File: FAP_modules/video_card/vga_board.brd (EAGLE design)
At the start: 100 x 75 mm, 32 parts, among them IC1 IS61LV256, IC2 IS61LV256

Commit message: added interrupt chaining and WAIT
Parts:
- moved U$2 12.4 mm to (3.05, 59.4)
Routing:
- net VGA_VSYNC: track 72.4 -> 84.3 mm
- net N$2: track 14.3 -> 25.8 mm
- net VGA_HSYNC: track 76.4 -> 87.6 mm
- net N$4: track 12.0 -> 18.8 mm
- net N$6: track 16.2 -> 14.2 mm
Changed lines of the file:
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@@
 <circle x="21.59" y="68.58" radius="2.032" width="0" layer="41"/>
 <circle x="92.71" y="68.58" radius="2.032" width="0" layer="41"/>
-<circle x="8.128" y="34.5186" radius="2.794" width="0" layer="41"/>
-<circle x="8.128" y="59.5884" radius="3.048" width="0" layer="41"/>
-<text x="1.27" y="65.2018" size="1.6764" layer="25" distance="70">FAP80 VGA
+<circle x="8.0772" y="46.8884" radius="2.794" width="0" layer="41"/>
+<circle x="8.0772" y="71.882" radius="3.048" width="0" layer="41"/>
+<text x="1.3716" y="29.1592" size="1.6764" layer="25" distance="70">FAP80 VGA
 Video Card REV2
 dekuNukem 2016</text>
@@
 <attribute name="NAME" x="27.051" y="54.0639" size="0.8128" layer="25" rot="R180"/>
 </element>
-<element name="U$2" library="SparkFun-Connectors" package="DB15" value="DB15" x="3.048" y="47.0154" smashed="yes" rot="R90"/>
+<element name="U$2" library="SparkFun-Connectors" package="DB15" value="DB15" x="3.048" y="59.4106" smashed="yes" rot="R90"/>
 <element name="U$1" library="cpu_board" package="FAP_BUS_2X38" value="FAP_BUS_FAP_BUS" x="32.258" y="2.032" smashed="yes"/>
 <element name="IC1" library="61lv256" package="SOJ28/3_LONGPAD" value="IS61LV256" x="46.228" y="51.816" smashed="yes" rot="R270">
@@
 <wire x1="22.341" y1="38.2524" x2="21.441" y2="37.3524" width="0.3048" layer="1"/>
 <wire x1="21.441" y1="37.3524" x2="19.558" y2="37.3524" width="0.3048" layer="1"/>
-<wire x1="19.558" y1="37.3524" x2="17.791" y2="37.3524" width="0.3048" layer="1"/>
-<wire x1="10.67" y1="42.6954" x2="10.668" y2="42.6954" width="0.3048" layer="1"/>
-<wire x1="17.791" y1="37.3524" x2="12.448" y2="42.6954" width="0.3048" layer="1"/>
-<wire x1="12.448" y1="42.6954" x2="10.668" y2="42.6954" width="0.3048" layer="1"/>
+<wire x1="19.558" y1="37.3524" x2="17.41" y2="37.3524" width="0.3048" layer="1"/>
+<wire x1="17.41" y1="37.3524" x2="15.2908" y2="39.4716" width="0.3048" layer="1"/>
+<wire x1="15.2908" y1="39.4716" x2="15.2908" y2="50.4678" width="0.3048" layer="1"/>
+<wire x1="15.2908" y1="50.4678" x2="10.668" y2="55.0906" width="0.3048" layer="1"/>
 </signal>
 <signal name="GND">
@@
 <wire x1="22.341" y1="45.8724" x2="19.569" y2="45.8724" width="0.3048" layer="1"/>
 <wire x1="19.569" y1="45.8724" x2="19.558" y2="45.8614" width="0.3048" layer="1"/>
-<wire x1="19.558" y1="45.8614" x2="18.682" y2="44.9854" width="0.3048" layer="1"/>
-<wire x1="18.682" y1="44.9854" x2="10.668" y2="44.9854" width="0.3048" layer="1"/>
+<wire x1="19.569" y1="45.8724" x2="18.2118" y2="45.8724" width="0.3048" layer="1"/>
+<wire x1="18.2118" y1="45.8724" x2="16.8402" y2="47.244" width="0.3048" layer="1"/>
+<wire x1="16.8402" y1="47.244" x2="16.8402" y2="51.2084" width="0.3048" layer="1"/>
+<wire x1="16.8402" y1="51.2084" x2="10.668" y2="57.3806" width="0.3048" layer="1"/>
 </signal>
 <signal name="N$5">
@@
 <wire x1="22.341" y1="53.6194" x2="22.33" y2="53.6084" width="0.3048" layer="1"/>
 <wire x1="22.33" y1="53.6084" x2="19.558" y2="53.6084" width="0.3048" layer="1"/>
-<wire x1="19.558" y1="53.6084" x2="19.039" y2="53.6084" width="0.3048" layer="1"/>
-<wire x1="19.039" y1="53.6084" x2="17.018" y2="51.5874" width="0.3048" layer="1"/>
-<wire x1="17.018" y1="51.5874" x2="17.018" y2="48.4124" width="0.3048" layer="1"/>
-<wire x1="10.674" y1="47.2694" x2="10.668" y2="47.2754" width="0.3048" layer="1"/>
-<wire x1="17.018" y1="48.4124" x2="15.881" y2="47.2754" width="0.3048" layer="1"/>
-<wire x1="15.881" y1="47.2754" x2="10.668" y2="47.2754" width="0.3048" layer="1"/>
+<wire x1="19.558" y1="53.6084" x2="18.2736" y2="53.6084" width="0.3048" layer="1"/>
+<wire x1="18.2736" y1="53.6084" x2="12.192" y2="59.69" width="0.3048" layer="1"/>
+<wire x1="12.192" y1="59.69" x2="10.6874" y2="59.69" width="0.3048" layer="1"/>
+<wire x1="10.6874" y1="59.69" x2="10.668" y2="59.6706" width="0.3048" layer="1"/>
 </signal>
 <signal name="+3V3">
@@
 <contactref element="U$2" pad="14"/>
 <contactref element="U$3" pad="23"/>
-<wire x1="1.651" y1="47.6504" x2="3.556" y2="49.5554" width="0.3048" layer="16"/>
-<wire x1="3.556" y1="49.5554" x2="5.578" y2="49.5554" width="0.3048" layer="16"/>
-<wire x1="5.578" y1="49.5554" x2="5.588" y2="49.5654" width="0.3048" layer="16"/>
 <wire x1="46.99" y1="15.24" x2="46.99" y2="17.8308" width="0.3048" layer="16"/>
 <wire x1="46.99" y1="17.8308" x2="46.101" y2="18.7198" width="0.3048" layer="16"/>
 <wire x1="46.101" y1="18.7198" x2="11.1506" y2="18.7198" width="0.3048" layer="16"/>
 <wire x1="11.1506" y1="18.7198" x2="1.651" y2="28.2194" width="0.3048" layer="16"/>
-<wire x1="1.651" y1="28.2194" x2="1.651" y2="47.6504" width="0.3048" layer="16"/>
+<wire x1="1.651" y1="28.2194" x2="1.651" y2="58.0236" width="0.3048" layer="16"/>
+<wire x1="1.651" y1="58.0236" x2="5.588" y2="61.9606" width="0.3048" layer="16"/>
 </signal>
 <signal name="VGA_VSYNC">
 <contactref element="U$2" pad="13"/>
 <contactref element="U$3" pad="21"/>
-<wire x1="3.0226" y1="45.593" x2="4.699" y2="47.2694" width="0.3048" layer="16"/>
-<wire x1="4.699" y1="47.2694" x2="5.582" y2="47.2694" width="0.3048" layer="16"/>
-<wire x1="5.582" y1="47.2694" x2="5.588" y2="47.2754" width="0.3048" layer="16"/>
 <wire x1="49.53" y1="15.24" x2="49.53" y2="17.3736" width="0.3048" layer="16"/>
 <wire x1="49.53" y1="17.3736" x2="47.0662" y2="19.8374" width="0.3048" layer="16"/>
 <wire x1="47.0662" y1="19.8374" x2="13.6652" y2="19.8374" width="0.3048" layer="16"/>
 <wire x1="13.6652" y1="19.8374" x2="3.0226" y2="30.48" width="0.3048" layer="16"/>
-<wire x1="3.0226" y1="30.48" x2="3.0226" y2="45.593" width="0.3048" layer="16"/>
+<wire x1="3.0226" y1="30.48" x2="3.0226" y2="57.1052" width="0.3048" layer="16"/>
+<wire x1="3.0226" y1="57.1052" x2="5.588" y2="59.6706" width="0.3048" layer="16"/>
 </signal>
 <signal name="+V">

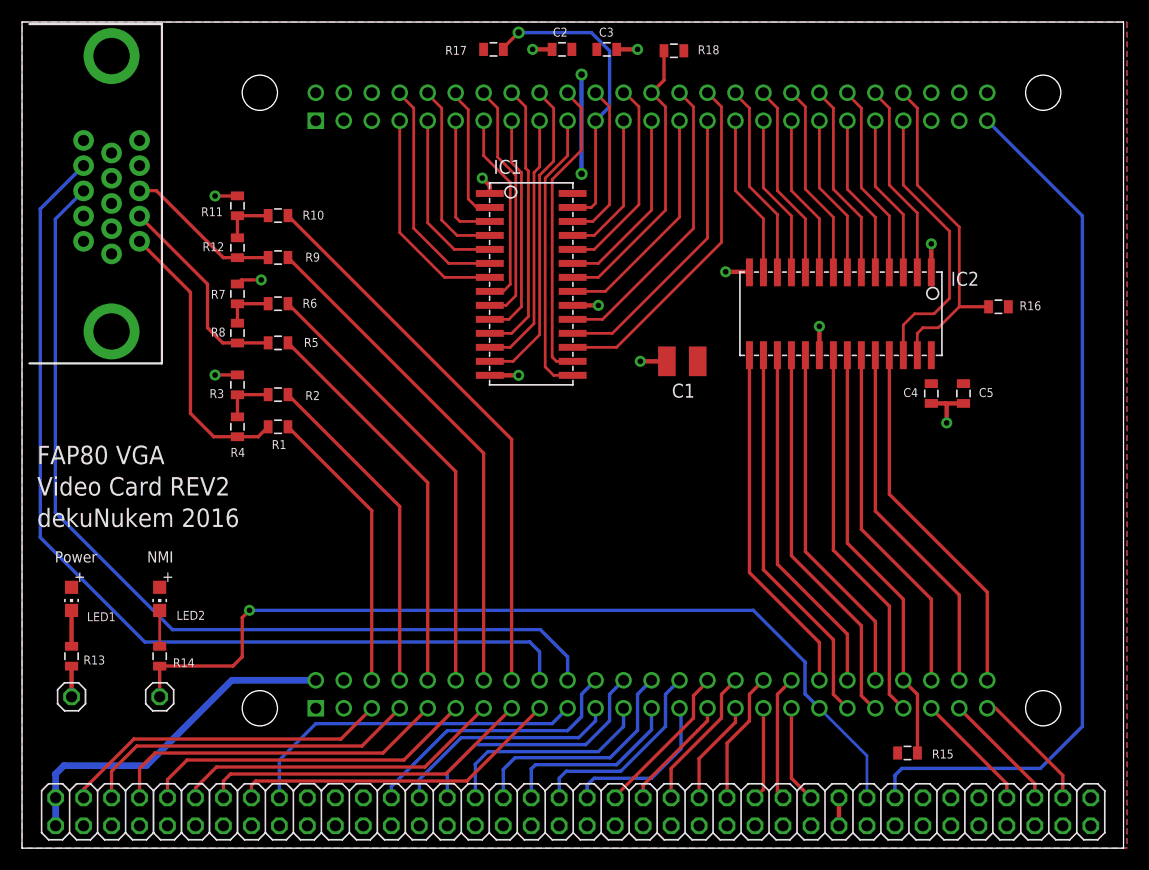
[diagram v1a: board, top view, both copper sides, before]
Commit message: moved VGA sockect
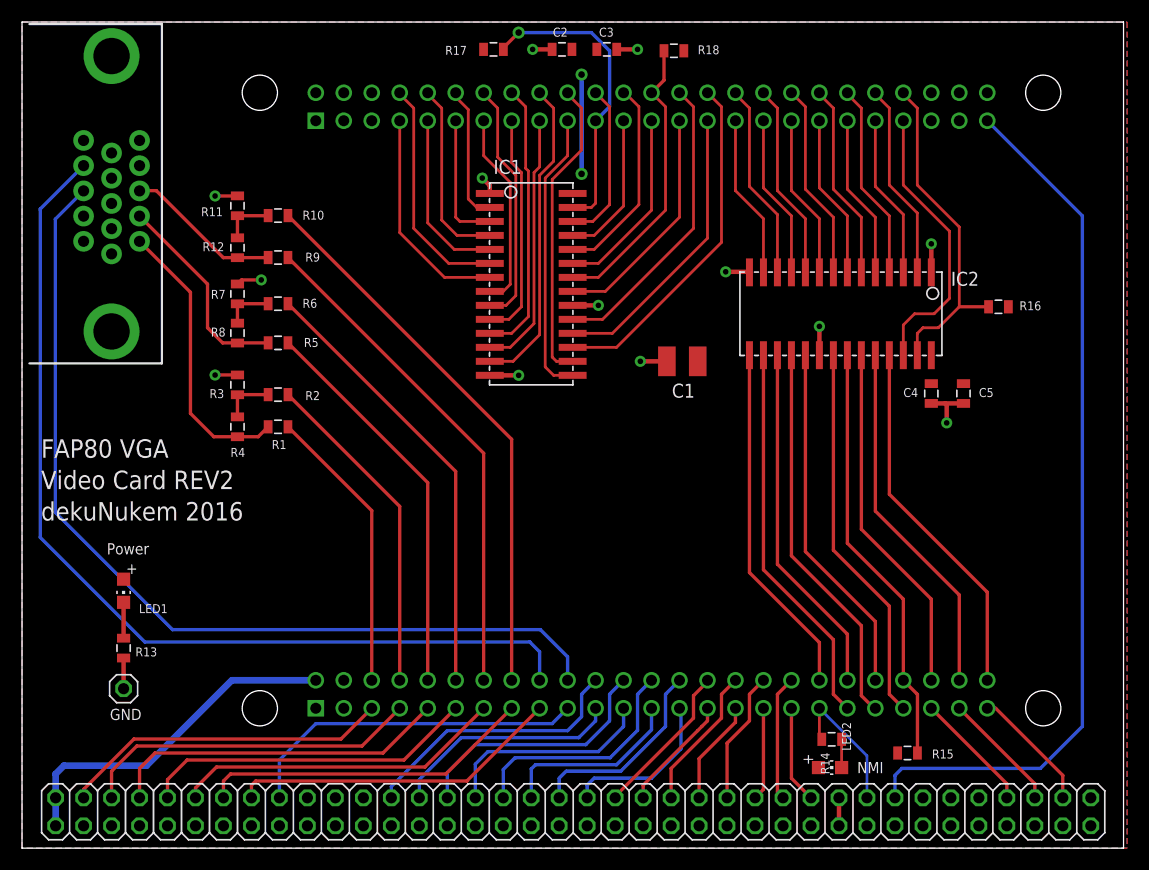
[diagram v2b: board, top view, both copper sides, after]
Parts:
- removed JP1: (no value), pinhead:1X01
- moved LED2 62.8 mm to (73.4, 7.32), turned to 270 degrees
- moved R14 61.5 mm to (73.5, 9.88), turned to 0 degrees
- moved JP2 4.78 mm to (9.22, 14.5)
- moved LED1 4.78 mm to (9.22, 23.4)
- moved R13 4.78 mm to (9.22, 18.2)
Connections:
- net N$36: no longer JP1.1
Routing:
- net N$36: track 82.2 -> 12.8 mm, vias 1 -> 0
- net N$35: track 3.26 -> 2.57 mm
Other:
- board text added: "GND"
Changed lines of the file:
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@@
 <circle x="8.0772" y="46.8884" radius="2.794" width="0" layer="41"/>
 <circle x="8.0772" y="71.882" radius="3.048" width="0" layer="41"/>
-<text x="1.3716" y="29.1592" size="1.6764" layer="25" distance="70">FAP80 VGA
+<text x="1.7272" y="29.7434" size="1.6764" layer="25" distance="70">FAP80 VGA
 Video Card REV2
 dekuNukem 2016</text>
-<text x="2.9718" y="25.9334" size="1.016" layer="25">Power</text>
-<text x="11.3538" y="25.9334" size="1.016" layer="25">NMI</text>
+<text x="7.6962" y="26.67" size="1.016" layer="25">Power</text>
+<text x="7.9756" y="11.6332" size="1.016" layer="25">GND</text>
+<text x="75.819" y="6.8072" size="1.016" layer="25">NMI</text>
 </plain>
 <attributes>
@@
 <attribute name="NAME" x="86.868" y="40.9575" size="0.8128" layer="25"/>
 </element>
-<element name="LED1" library="cpu_board" package="CHIP-LED0805" value="" x="4.4958" y="22.6314" smashed="yes" rot="R180">
-<attribute name="NAME" x="5.8928" y="20.5994" size="0.8128" layer="25"/>
-<attribute name="VALUE" x="1.9558" y="23.9014" size="1.27" layer="27" rot="R270"/>
-</element>
-<element name="R13" library="cpu_board" package="0805" value="" x="4.4958" y="17.4244" smashed="yes" rot="R90">
-<attribute name="NAME" x="7.5438" y="17.4879" size="0.8128" layer="25" rot="R180"/>
-<attribute name="VALUE" x="5.8928" y="16.4084" size="0.4064" layer="27" rot="R90"/>
-</element>
-<element name="LED2" library="cpu_board" package="CHIP-LED0805" value="" x="12.4968" y="22.6314" smashed="yes" rot="R180">
-<attribute name="NAME" x="14.0208" y="20.7264" size="0.8128" layer="25"/>
-<attribute name="VALUE" x="9.9568" y="23.9014" size="1.27" layer="27" rot="R270"/>
-</element>
-<element name="R14" library="cpu_board" package="0805" value="" x="12.4968" y="17.4244" smashed="yes" rot="R90">
-<attribute name="NAME" x="15.6718" y="17.2339" size="0.8128" layer="25" rot="R180"/>
-<attribute name="VALUE" x="13.8938" y="16.4084" size="0.4064" layer="27" rot="R90"/>
-</element>
-<element name="JP1" library="pinhead" package="1X01" value="" x="12.4968" y="13.7414" smashed="yes">
-<attribute name="VALUE" x="11.2268" y="10.5664" size="1.27" layer="27"/>
-</element>
-<element name="JP2" library="pinhead" package="1X01" value="" x="4.4958" y="13.7414" smashed="yes">
-<attribute name="VALUE" x="3.2258" y="10.5664" size="1.27" layer="27"/>
+<element name="LED1" library="cpu_board" package="CHIP-LED0805" value="" x="9.2202" y="23.368" smashed="yes" rot="R180">
+<attribute name="NAME" x="10.6172" y="21.336" size="0.8128" layer="25"/>
+<attribute name="VALUE" x="6.6802" y="24.638" size="1.27" layer="27" rot="R270"/>
+</element>
+<element name="R13" library="cpu_board" package="0805" value="" x="9.2202" y="18.161" smashed="yes" rot="R90">
+<attribute name="NAME" x="12.2682" y="18.2245" size="0.8128" layer="25" rot="R180"/>
+<attribute name="VALUE" x="10.6172" y="17.145" size="0.4064" layer="27" rot="R90"/>
+</element>
+<element name="LED2" library="cpu_board" package="CHIP-LED0805" value="" x="73.3552" y="7.3152" smashed="yes" rot="R270">
+<attribute name="NAME" x="75.2602" y="8.8392" size="0.8128" layer="25" rot="R90"/>
+<attribute name="VALUE" x="72.0852" y="4.7752" size="1.27" layer="27"/>
+</element>
+<element name="R14" library="cpu_board" package="0805" value="" x="73.5076" y="9.8806" smashed="yes">
+<attribute name="NAME" x="73.3171" y="6.7056" size="0.8128" layer="25" rot="R90"/>
+<attribute name="VALUE" x="72.4916" y="8.4836" size="0.4064" layer="27"/>
+</element>
+<element name="JP2" library="pinhead" package="1X01" value="" x="9.2202" y="14.478" smashed="yes">
+<attribute name="VALUE" x="7.9502" y="11.303" size="1.27" layer="27"/>
 </element>
 <element name="R15" library="cpu_board" package="0805" value="" x="80.391" y="8.636" smashed="yes" rot="R180">
@@
 <wire x1="83.947" y1="40.248" x2="83.82" y2="40.375" width="0.4064" layer="1"/>
 <contactref element="JP2" pad="1"/>
-<wire x1="4.4958" y1="13.7414" x2="4.4958" y2="16.5244" width="0.4064" layer="1"/>
+<wire x1="9.2202" y1="14.478" x2="9.2202" y2="17.261" width="0.4064" layer="1"/>
 </signal>
 <signal name="N$3">
@@
 <contactref element="LED1" pad="C"/>
 <contactref element="R13" pad="2"/>
-<wire x1="4.4958" y1="21.5814" x2="4.4958" y2="18.3244" width="0.4064" layer="1"/>
+<wire x1="9.2202" y1="22.318" x2="9.2202" y2="19.061" width="0.4064" layer="1"/>
 </signal>
 <signal name="N$36">
 <contactref element="U$3" pad="142"/>
-<contactref element="JP1" pad="1"/>
 <contactref element="U$1" pad="NMI"/>
 <wire x1="76.708" y1="4.572" x2="76.708" y2="8.382" width="0.254" layer="16"/>
 <wire x1="76.708" y1="8.382" x2="72.39" y2="12.7" width="0.254" layer="16"/>
 <contactref element="R14" pad="1"/>
-<wire x1="12.4858" y1="16.5354" x2="12.4968" y2="16.5244" width="0.254" layer="1"/>
-<wire x1="12.4858" y1="16.5354" x2="19.1516" y2="16.5354" width="0.3048" layer="1"/>
-<wire x1="19.1516" y1="16.5354" x2="19.9898" y2="17.3736" width="0.3048" layer="1"/>
-<wire x1="19.9898" y1="17.3736" x2="19.9898" y2="20.9296" width="0.3048" layer="1"/>
-<wire x1="19.9898" y1="20.9296" x2="20.6502" y2="21.59" width="0.3048" layer="1"/>
-<via x="20.6502" y="21.59" extent="1-16" drill="0.5"/>
-<wire x1="20.6502" y1="21.59" x2="66.3956" y2="21.59" width="0.3048" layer="16"/>
-<wire x1="66.3956" y1="21.59" x2="71.0946" y2="16.891" width="0.3048" layer="16"/>
-<wire x1="71.0946" y1="16.891" x2="71.0946" y2="13.9954" width="0.3048" layer="16"/>
-<wire x1="71.0946" y1="13.9954" x2="72.39" y2="12.7" width="0.3048" layer="16"/>
-<wire x1="12.4968" y1="13.7414" x2="12.4968" y2="16.5244" width="0.3048" layer="1"/>
+<wire x1="72.39" y1="12.7" x2="72.39" y2="10.0982" width="0.254" layer="1"/>
+<wire x1="72.39" y1="10.0982" x2="72.6076" y2="9.8806" width="0.254" layer="1"/>
 </signal>
 <signal name="N$37">
@@
 <contactref element="LED2" pad="C"/>
 <contactref element="R14" pad="2"/>
-<wire x1="12.4968" y1="18.3244" x2="12.4968" y2="21.5814" width="0.254" layer="1"/>
+<wire x1="74.4076" y1="9.8806" x2="74.4076" y2="7.3176" width="0.254" layer="1"/>
+<wire x1="74.4076" y1="7.3176" x2="74.4052" y2="7.3152" width="0.254" layer="1"/>
 </signal>
 <signal name="N$38">

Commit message: board cleanup
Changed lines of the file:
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@@
 <circle x="8.0772" y="46.8884" radius="2.794" width="0" layer="41"/>
 <circle x="8.0772" y="71.882" radius="3.048" width="0" layer="41"/>
-<text x="1.7272" y="29.7434" size="1.6764" layer="25" distance="70">FAP80 VGA
+<text x="0.8636" y="28.9052" size="1.6764" layer="25" distance="70">FAP80 VGA
 Video Card REV2
 dekuNukem 2016</text>

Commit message: added all Z80 signals on bus
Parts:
- U$1: value FAP_BUS_FAP_BUS -> FAP_BUS; device cpu_board:FAP_BUS_2X38 -> fap_bus:2X38
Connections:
- net GND: no longer U$1.GND@31, U$1.GND@33
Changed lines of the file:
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@@
 </element>
 <element name="U$2" library="SparkFun-Connectors" package="DB15" value="DB15" x="3.048" y="59.4106" smashed="yes" rot="R90"/>
-<element name="U$1" library="cpu_board" package="FAP_BUS_2X38" value="FAP_BUS_FAP_BUS" x="32.258" y="2.032" smashed="yes"/>
+<element name="U$1" library="fap_bus" package="2X38" value="FAP_BUS" x="32.258" y="2.032" smashed="yes"/>
 <element name="IC1" library="61lv256" package="SOJ28/3_LONGPAD" value="IS61LV256" x="46.228" y="51.816" smashed="yes" rot="R270">
 <attribute name="NAME" x="42.799" y="61.214" size="1.27" layer="25"/>
@@
 <contactref element="U$1" pad="GND@13"/>
 <contactref element="U$1" pad="GND@23"/>
-<contactref element="U$1" pad="GND@31"/>
 <contactref element="U$1" pad="GND@35"/>
 <contactref element="U$1" pad="GND@16"/>
@@
 <contactref element="U$1" pad="GND@20"/>
 <contactref element="U$1" pad="GND@26"/>
-<contactref element="U$1" pad="GND@33"/>
 <contactref element="U$1" pad="GND@24"/>
 <contactref element="U$1" pad="GND@38"/>

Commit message: board cleanup
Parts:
- added JP1: JUMPER-PAD-2-NO, SparkFun-Passives:PAD-JUMPER-2-NO_NO_SILK
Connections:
- new net N$39: JP1.1, U$1.NMI
- net N$36: now also JP1.2; no longer U$1.NMI
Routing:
- net N$39: track 0.00 -> 3.39 mm
- net N$36: track 12.8 -> 9.65 mm
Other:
- board text added: "FAP80 VGA Video Card V2 dekuNukem 2016"
- board text removed: "FAP80 VGA Video Card REV2 dekuNukem 2016"
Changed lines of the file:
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@@
 <circle x="8.0772" y="71.882" radius="3.048" width="0" layer="41"/>
 <text x="0.8636" y="28.9052" size="1.6764" layer="25" distance="70">FAP80 VGA
-Video Card REV2
+Video Card V2
 dekuNukem 2016</text>
 <text x="7.6962" y="26.67" size="1.016" layer="25">Power</text>
@@
 <attribute name="VALUE" x="58.166" y="70.993" size="0.4064" layer="27"/>
 </element>
+<element name="JP1" library="SparkFun-Passives" package="PAD-JUMPER-2-NO_NO_SILK" value="JUMPER-PAD-2-NO" x="76.708" y="8.4074" rot="MR90"/>
 </elements>
 <signals>
@@
 <signal name="N$36">
 <contactref element="U$3" pad="142"/>
-<contactref element="U$1" pad="NMI"/>
-<wire x1="76.708" y1="4.572" x2="76.708" y2="8.382" width="0.254" layer="16"/>
-<wire x1="76.708" y1="8.382" x2="72.39" y2="12.7" width="0.254" layer="16"/>
 <contactref element="R14" pad="1"/>
 <wire x1="72.39" y1="12.7" x2="72.39" y2="10.0982" width="0.254" layer="1"/>
 <wire x1="72.39" y1="10.0982" x2="72.6076" y2="9.8806" width="0.254" layer="1"/>
+<contactref element="JP1" pad="2"/>
+<wire x1="76.708" y1="8.8574" x2="74.8102" y2="8.8574" width="0.4064" layer="16"/>
+<wire x1="74.8102" y1="8.8574" x2="72.39" y2="11.2776" width="0.4064" layer="16"/>
+<wire x1="72.39" y1="11.2776" x2="72.39" y2="12.7" width="0.4064" layer="16"/>
 </signal>
 <signal name="N$37">
@@
 <wire x1="74.168" y1="4.572" x2="74.168" y2="2.032" width="0.4064" layer="1"/>
 </signal>
+<signal name="N$39">
+<contactref element="U$1" pad="NMI"/>
+<contactref element="JP1" pad="1"/>
+<wire x1="76.708" y1="4.572" x2="76.708" y2="7.9574" width="0.4064" layer="16"/>
+</signal>
 </signals>
